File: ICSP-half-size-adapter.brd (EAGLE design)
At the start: 13 x 9.5 mm, 2 parts

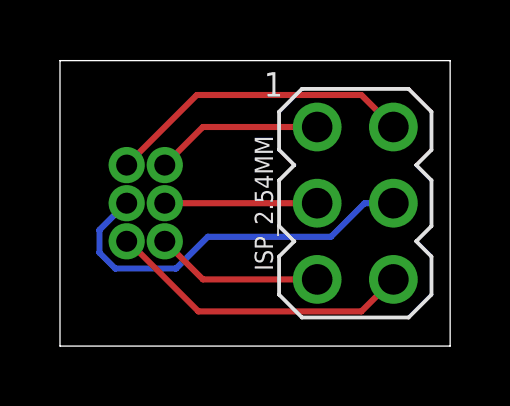
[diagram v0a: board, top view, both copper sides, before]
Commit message: Un-mirror 0.05" pads: thanks @bschulz1701
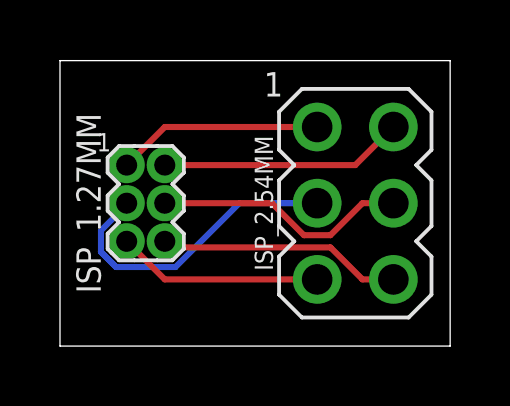
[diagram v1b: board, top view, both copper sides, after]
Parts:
- flipped ISP_1.27MM to the top
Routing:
- net SCK: track 5.08 -> 10.3 mm
- net MOSI: track 13.0 -> 8.50 mm
- net VCC: track 10.3 -> 8.15 mm
- net GND: track 10.3 -> 8.15 mm
- net RST: track 5.61 -> 6.88 mm
- net MISO: track 5.61 -> 6.88 mm
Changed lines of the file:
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@@
 <layer number="50" name="dxf" color="7" fill="1" visible="no" active="no"/>
 <layer number="51" name="tDocu" color="7" fill="1" visible="yes" active="yes"/>
-<layer number="52" name="bDocu" color="7" fill="1" visible="no" active="yes"/>
+<layer number="52" name="bDocu" color="7" fill="1" visible="yes" active="yes"/>
 <layer number="53" name="tGND_GNDA" color="7" fill="9" visible="no" active="no"/>
 <layer number="54" name="bGND_GNDA" color="1" fill="9" visible="no" active="no"/>
@@
 </autorouter>
 <elements>
-<element name="ISP_1.27MM" library="bschulz" package="2X3_1.27" value="AVRISP1.27MM" x="2.8575" y="4.7625" smashed="yes" rot="MR270">
-<attribute name="NAME" x="4.7625" y="4.7625" size="0.8128" layer="26" font="vector" ratio="15" rot="MR90" align="center"/>
+<element name="ISP_1.27MM" library="bschulz" package="2X3_1.27" value="AVRISP1.27MM" x="2.8575" y="4.7625" smashed="yes" rot="R270">
+<attribute name="NAME" x="0.9525" y="4.7625" size="0.8128" layer="25" font="vector" ratio="15" rot="R90" align="center"/>
 </element>
 <element name="ISP_2.54MM" library="bschulz" package="AVRISP" value="AVRISP-6" x="9.8425" y="4.7625" smashed="yes">
@@
 <contactref element="ISP_2.54MM" pad="4"/>
 <contactref element="ISP_1.27MM" pad="4"/>
-<wire x1="1.8460625" y1="2.5837" x2="1.3137" y2="3.1160625" width="0.2032" layer="16"/>
-<wire x1="1.3137" y1="3.1160625" x2="1.3137" y2="3.8689375" width="0.2032" layer="16"/>
-<wire x1="1.3137" y1="3.8689375" x2="1.8460625" y2="4.4013" width="0.2032" layer="16"/>
-<wire x1="11.1125" y1="4.7625" x2="10.15303125" y2="4.7625" width="0.2032" layer="16"/>
-<wire x1="10.15303125" y1="4.7625" x2="9.03543125" y2="3.6449" width="0.2032" layer="16"/>
-<wire x1="3.8689375" y1="2.5837" x2="1.8460625" y2="2.5837" width="0.2032" layer="16"/>
-<wire x1="1.8460625" y1="4.4013" x2="1.8613" y2="4.4013" width="0.2032" layer="16"/>
-<wire x1="1.8613" y1="4.4013" x2="2.2225" y2="4.7625" width="0.2032" layer="16"/>
-<wire x1="9.03543125" y1="3.6449" x2="4.9301375" y2="3.6449" width="0.2032" layer="16"/>
-<wire x1="4.9301375" y1="3.6449" x2="3.8689375" y2="2.5837" width="0.2032" layer="16"/>
+<wire x1="9.0143875" y1="3.6957" x2="8.1306125" y2="3.6957" width="0.2032" layer="1"/>
+<wire x1="11.1125" y1="4.7625" x2="10.0811875" y2="4.7625" width="0.2032" layer="1"/>
+<wire x1="7.0638125" y1="4.7625" x2="3.4925" y2="4.7625" width="0.2032" layer="1"/>
+<wire x1="10.0811875" y1="4.7625" x2="9.0143875" y2="3.6957" width="0.2032" layer="1"/>
+<wire x1="8.1306125" y1="3.6957" x2="7.0638125" y2="4.7625" width="0.2032" layer="1"/>
 </signal>
 <signal name="GND">
 <contactref element="ISP_1.27MM" pad="6"/>
 <contactref element="ISP_2.54MM" pad="6"/>
-<wire x1="2.2225" y1="3.4925" x2="2.2791" y2="3.4925" width="0.2032" layer="1"/>
-<wire x1="2.2791" y1="3.4925" x2="4.6159" y2="1.1557" width="0.2032" layer="1"/>
-<wire x1="10.0457" y1="1.1557" x2="11.1125" y2="2.2225" width="0.2032" layer="1"/>
-<wire x1="4.6159" y1="1.1557" x2="10.0457" y2="1.1557" width="0.2032" layer="1"/>
+<wire x1="11.1125" y1="2.2225" x2="10.0811875" y2="2.2225" width="0.2032" layer="1"/>
+<wire x1="10.0811875" y1="2.2225" x2="9.0143875" y2="3.2893" width="0.2032" layer="1"/>
+<wire x1="3.6957" y1="3.2893" x2="3.4925" y2="3.4925" width="0.2032" layer="1"/>
+<wire x1="9.0143875" y1="3.2893" x2="3.6957" y2="3.2893" width="0.2032" layer="1"/>
 </signal>
 <signal name="VCC">
 <contactref element="ISP_1.27MM" pad="2"/>
 <contactref element="ISP_2.54MM" pad="2"/>
-<wire x1="2.2225" y1="6.0325" x2="4.5593" y2="8.3693" width="0.2032" layer="1"/>
-<wire x1="10.0457" y1="8.3693" x2="11.1125" y2="7.3025" width="0.2032" layer="1"/>
-<wire x1="4.5593" y1="8.3693" x2="10.0457" y2="8.3693" width="0.2032" layer="1"/>
+<wire x1="3.4925" y1="6.0325" x2="9.8425" y2="6.0325" width="0.2032" layer="1"/>
+<wire x1="9.8425" y1="6.0325" x2="11.1125" y2="7.3025" width="0.2032" layer="1"/>
 </signal>
 <signal name="MISO">
 <contactref element="ISP_1.27MM" pad="1"/>
 <contactref element="ISP_2.54MM" pad="1"/>
-<wire x1="3.4925" y1="6.0325" x2="4.7625" y2="7.3025" width="0.2032" layer="1"/>
-<wire x1="4.7625" y1="7.3025" x2="8.5725" y2="7.3025" width="0.2032" layer="1"/>
+<wire x1="2.2225" y1="6.0325" x2="3.4925" y2="7.3025" width="0.2032" layer="1"/>
+<wire x1="3.4925" y1="7.3025" x2="8.5725" y2="7.3025" width="0.2032" layer="1"/>
 </signal>
 <signal name="SCK">
 <contactref element="ISP_1.27MM" pad="3"/>
 <contactref element="ISP_2.54MM" pad="3"/>
-<wire x1="8.5725" y1="4.7625" x2="3.4925" y2="4.7625" width="0.2032" layer="1"/>
+<wire x1="1.8671" y1="2.6345" x2="1.3645" y2="3.1371" width="0.2032" layer="16"/>
+<wire x1="1.3645" y1="3.1371" x2="1.3645" y2="3.8479" width="0.2032" layer="16"/>
+<wire x1="3.8479" y1="2.6345" x2="1.8671" y2="2.6345" width="0.2032" layer="16"/>
+<wire x1="8.5725" y1="4.7625" x2="5.9759" y2="4.7625" width="0.2032" layer="16"/>
+<wire x1="5.9759" y1="4.7625" x2="3.8479" y2="2.6345" width="0.2032" layer="16"/>
+<wire x1="2.2225" y1="4.7059" x2="2.2225" y2="4.7625" width="0.2032" layer="16"/>
+<wire x1="1.3645" y1="3.8479" x2="2.2225" y2="4.7059" width="0.2032" layer="16"/>
 </signal>
 <signal name="RST">
 <contactref element="ISP_1.27MM" pad="5"/>
 <contactref element="ISP_2.54MM" pad="5"/>
-<wire x1="8.5725" y1="2.2225" x2="4.7625" y2="2.2225" width="0.2032" layer="1"/>
-<wire x1="4.7625" y1="2.2225" x2="3.4925" y2="3.4925" width="0.2032" layer="1"/>
+<wire x1="8.5725" y1="2.2225" x2="3.4925" y2="2.2225" width="0.2032" layer="1"/>
+<wire x1="3.4925" y1="2.2225" x2="2.2225" y2="3.4925" width="0.2032" layer="1"/>
 </signal>
 </signals>
